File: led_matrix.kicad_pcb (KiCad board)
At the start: 2 copper layers, 63.5 x 63.5 mm, 82 parts, among them J1 Conn_01x08_Male, J2 Conn_01x08_Male

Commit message: Finish Rev C PCB
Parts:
- removed J2: Conn_01x08_Male, Connector_PinHeader_1.27mm:PinHeader_1x08_P1.27mm_Vertical
- removed R10, R11, R12, R13, R14, R15, R16, R3, R4, R5, R6, R7, R8, R9: 120, Resistor_SMD:R_0603_1608Metric
- added C1: 10uF, Capacitor_SMD:CP_Elec_6.3x3, F.Cu at (136.7, 116.8)
- added C2: 100nF, Capacitor_SMD:C_0603_1608Metric, F.Cu at (165.1, 110.0)
- added U1: MAX7219, Package_SO:SOP-24_7.5x15.4mm_P1.27mm, F.Cu at (164.6, 116.8)
- J1: value Conn_01x08_Male -> Conn_01x05_Male; footprint Connector_PinHeader_1.27mm:PinHeader_1x08_P1.27mm_Vertical -> Connector_PinHeader_1.27mm:PinHeader_1x05_P1.27mm_Vertical
- R1: value 120 -> 27k
- R2: value 120 -> 10k
- moved R2 132.5 mm to (170.7, 123.7), turned to 180 degrees
- moved R1 118.7 mm to (154.9, 116.6), turned to 0 degrees
- moved J1 105.6 mm to (150.6, 116.8)
- moved D1 93.7 mm to (139.4, 81.3)
- moved D9 92.9 mm to (139.4, 84.8)
- moved D17 92.1 mm to (139.4, 88.4)
- moved D25 91.4 mm to (139.4, 91.9)
- moved D2 91.1 mm to (143.0, 81.3)
- moved D33 90.7 mm to (139.4, 95.5)
- moved D10 90.2 mm to (143.0, 84.8)
- moved D41 90.2 mm to (139.4, 99.1)
- moved D49 89.7 mm to (139.4, 102.6)
- moved D18 89.4 mm to (143.0, 88.4)
- moved D57 89.3 mm to (139.4, 106.2)
- moved D26 88.7 mm to (143.0, 91.9)
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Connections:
- net Net-(D1-Pad1) renamed /matr0
- net Net-(D10-Pad1) renamed /matr1
- net Net-(D11-Pad2) renamed /matc2
- net Net-(D12-Pad2) renamed /matc3
- net Net-(D13-Pad2) renamed /matc4
- net Net-(D14-Pad2) renamed /matc5
- net Net-(D15-Pad2) renamed /matc6
- net Net-(D16-Pad2) renamed /matc7
- net Net-(D17-Pad1) renamed /matr2
- net Net-(D25-Pad1) renamed /matr3
- net Net-(D33-Pad1) renamed /matr4
- net Net-(D41-Pad1) renamed /matr5
- net Net-(D49-Pad1) renamed /matr6
- net Net-(D57-Pad1) renamed /matr7
- D1 pad 2: Net-(D1-Pad2) -> /matc0
- D10 pad 2: Net-(D10-Pad2) -> /matc1
- D17 pad 2: Net-(D1-Pad2) -> /matc0
- D18 pad 2: Net-(D10-Pad2) -> /matc1
- D2 pad 2: Net-(D10-Pad2) -> /matc1
- D25 pad 2: Net-(D1-Pad2) -> /matc0
- D26 pad 2: Net-(D10-Pad2) -> /matc1
- D33 pad 2: Net-(D1-Pad2) -> /matc0
- D34 pad 2: Net-(D10-Pad2) -> /matc1
- D41 pad 2: Net-(D1-Pad2) -> /matc0
- D42 pad 2: Net-(D10-Pad2) -> /matc1
- D49 pad 2: Net-(D1-Pad2) -> /matc0
- D50 pad 2: Net-(D10-Pad2) -> /matc1
- D57 pad 2: Net-(D1-Pad2) -> /matc0
- D58 pad 2: Net-(D10-Pad2) -> /matc1
- D9 pad 2: Net-(D1-Pad2) -> /matc0
- J1 pad 1: Net-(J1-Pad1) -> DIN
- J1 pad 2: Net-(J1-Pad2) -> CLK
- J1 pad 3: Net-(J1-Pad3) -> LOAD
- J1 pad 4: Net-(J1-Pad4) -> +5V
- J1 pad 5: Net-(J1-Pad5) -> GND
- R1 pad 1: Net-(D1-Pad2) -> +5V
- R1 pad 2: Net-(J1-Pad8) -> Net-(R1-Pad2)
- R2 pad 1: Net-(D10-Pad2) -> LOAD
- R2 pad 2: Net-(J1-Pad7) -> GND
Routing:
- net /matc1: track 0.00 -> 98.0 mm
- net Net-(D1-Pad2): track 79.9 -> 0.00 mm
- net Net-(D10-Pad2): track 76.9 -> 0.00 mm
- net /matc0: track 0.00 -> 73.8 mm, vias 0 -> 2
- net +5V: track 0.00 -> 39.4 mm
- net /matc7: track 79.4 -> 45.9 mm
- net LOAD: track 0.00 -> 31.1 mm
- net CLK: track 0.00 -> 26.7 mm
- net /matc3: track 74.6 -> 51.3 mm
- net /matc4: track 74.6 -> 52.0 mm
- net /matr2: track 66.2 -> 86.4 mm, vias 8 -> 9
- net /matc5: track 74.6 -> 54.8 mm, vias 0 -> 2
- net /matr3: track 66.2 -> 86.0 mm, vias 8 -> 11
- net /matr7: track 70.6 -> 51.5 mm, vias 8 -> 9
- net /matr0: track 70.6 -> 86.0 mm, vias 8 -> 11
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- added copper zone on B.Cu, net GND
- added copper zone on F.Cu, net GND
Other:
- board size 63.5 x 63.5 mm -> 43.9 x 48.8 mm
- board text added: "CLK"
- board text added: "DIN"
- board text added: "GND"
- board text added: "LOAD"
- board text added: "V+"

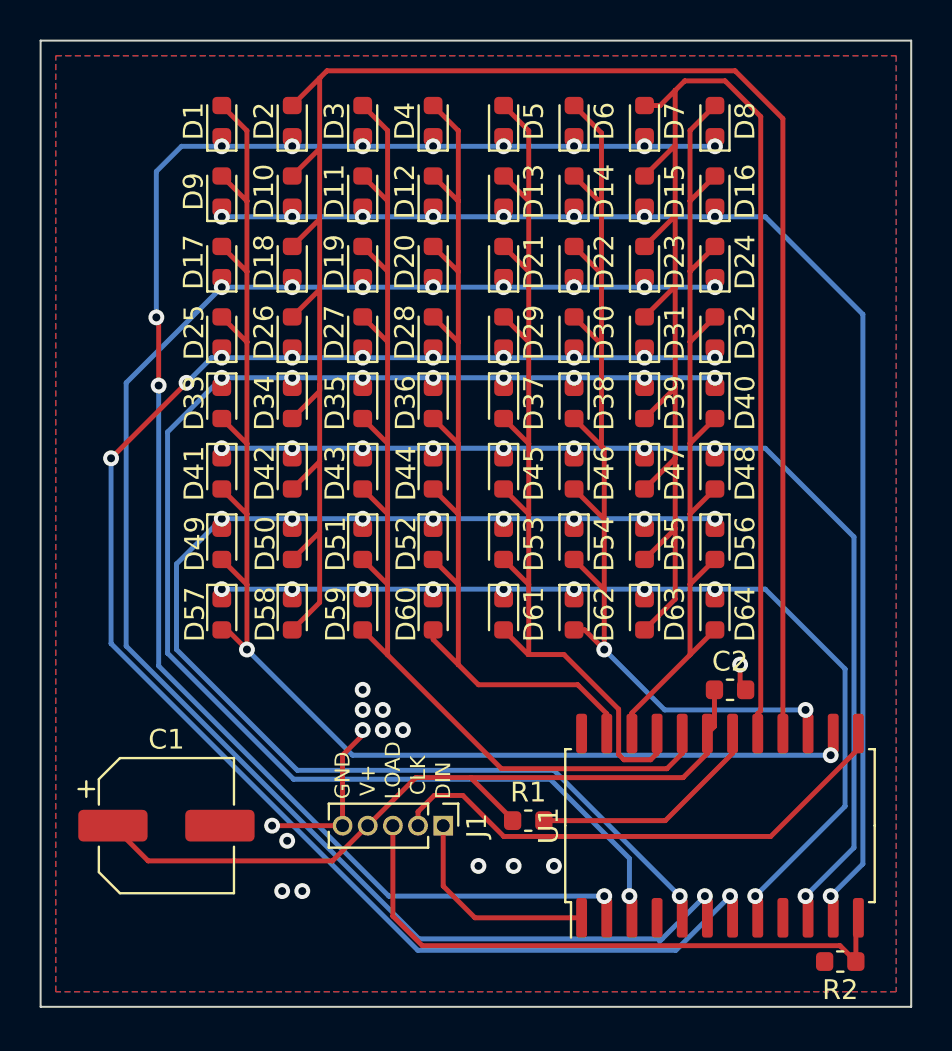
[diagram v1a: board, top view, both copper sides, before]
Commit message: Upgrade to 4 Layer PCB
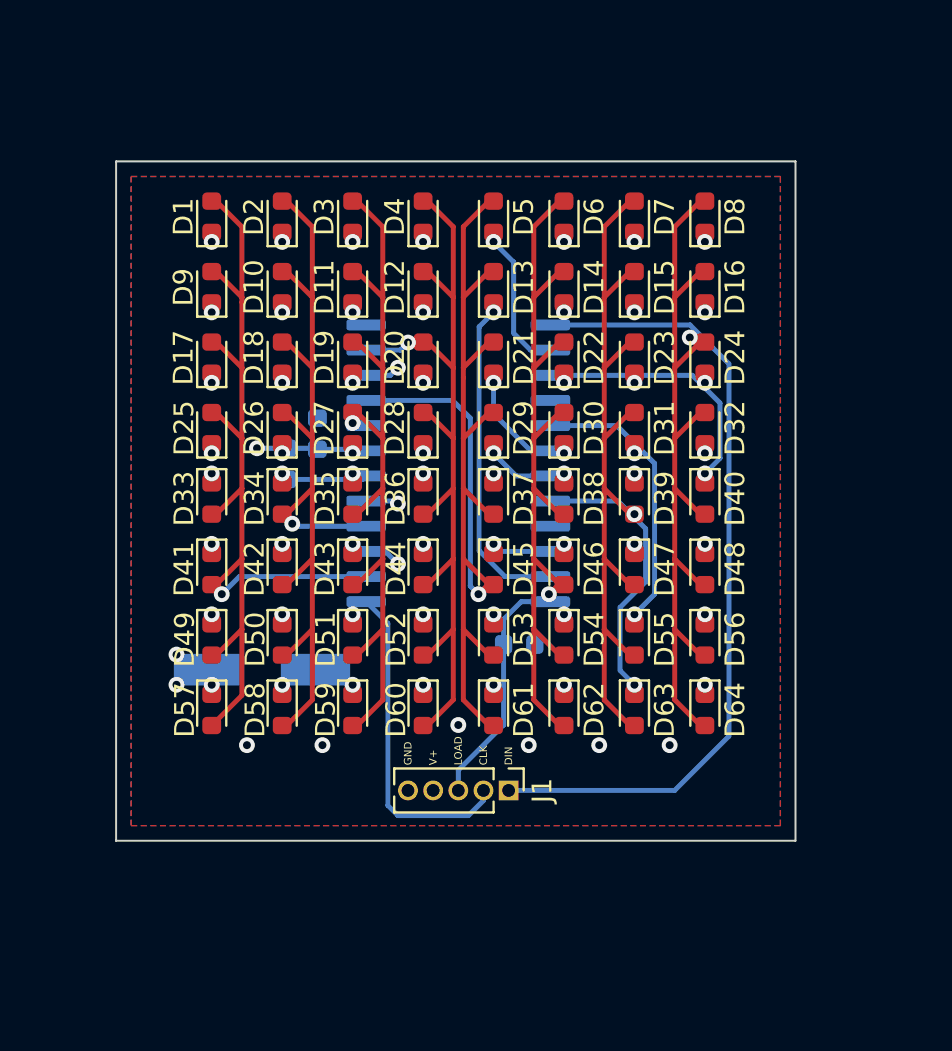
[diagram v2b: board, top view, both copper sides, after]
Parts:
- C1, C2, R1, R2, U1: moved to B.Cu
- moved C2 24.5 mm to (144.3, 97.1), turned to 90 degrees
- moved R2 22.8 mm to (154.5, 107.7), turned to 0 degrees
- moved U1 22.6 mm to (151.4, 98.6), turned to 180 degrees
- moved R1 21.7 mm to (142.7, 98.6), turned to 270 degrees
- moved C1 9.24 mm to (141.5, 109.0)
- moved D10 4.85 mm to (142.5, 89.7)
- moved D12 4.85 mm to (149.6, 89.7)
- moved D14 4.85 mm to (156.7, 89.7)
- moved D15 4.85 mm to (160.3, 89.7)
- moved D17 4.85 mm to (138.9, 93.2)
- moved D18 4.85 mm to (142.5, 93.2)
- moved D20 4.85 mm to (149.6, 93.2)
- moved D22 4.85 mm to (156.7, 93.2)
- moved D23 4.85 mm to (160.3, 93.2)
- moved D25 4.85 mm to (138.9, 96.8)
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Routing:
- net /matr3: track 86.0 -> 32.1 mm, vias 11 -> 8
- net /matc1: track 98.0 -> 44.9 mm, vias 0 -> 1
- net /matr2: track 86.4 -> 34.0 mm, vias 9 -> 8
- net /matr0: track 86.0 -> 36.0 mm, vias 11 -> 8
- net +5V: track 39.4 -> 5.67 mm, vias 0 -> 3
- net /matr4: track 74.4 -> 41.8 mm, vias 9 -> 8
- net DIN: track 10.7 -> 40.9 mm
- net /matr5: track 57.9 -> 31.8 mm, vias 9 -> 8
- net /matc6: track 79.4 -> 54.2 mm, vias 0 -> 2
- net /matr6: track 68.0 -> 42.8 mm, vias 9 -> 8
- net /matc0: track 73.8 -> 48.6 mm, vias 2 -> 1
- net /matr1: track 69.4 -> 45.2 mm, vias 9 -> 8
- net LOAD: track 31.1 -> 12.3 mm
- net /matc2: track 59.3 -> 41.6 mm, vias 0 -> 1
- net /matc7: track 45.9 -> 58.3 mm, vias 0 -> 2
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- added copper zone on In2.Cu, net +5V
- added copper zone on In1.Cu, net GND
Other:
- board size 43.9 x 48.8 mm -> 34.3 x 34.3 mm
- copper layers 2 -> 4
